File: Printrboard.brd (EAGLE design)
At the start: 100.1 x 61 mm, 119 parts, among them J1 MICROSD, J2 USB-MICROB, J3 ATX, Q1 RFP30N06LE, Q2 RFP30N06LE, Q3 RFP30N06LE, U1 LM2841, U2 A4982, U3 A4982, U4 A4982, U5 A4982, U6 AT90USB1286, U7 AP7313, U8 TXB0104, X1 8MHz

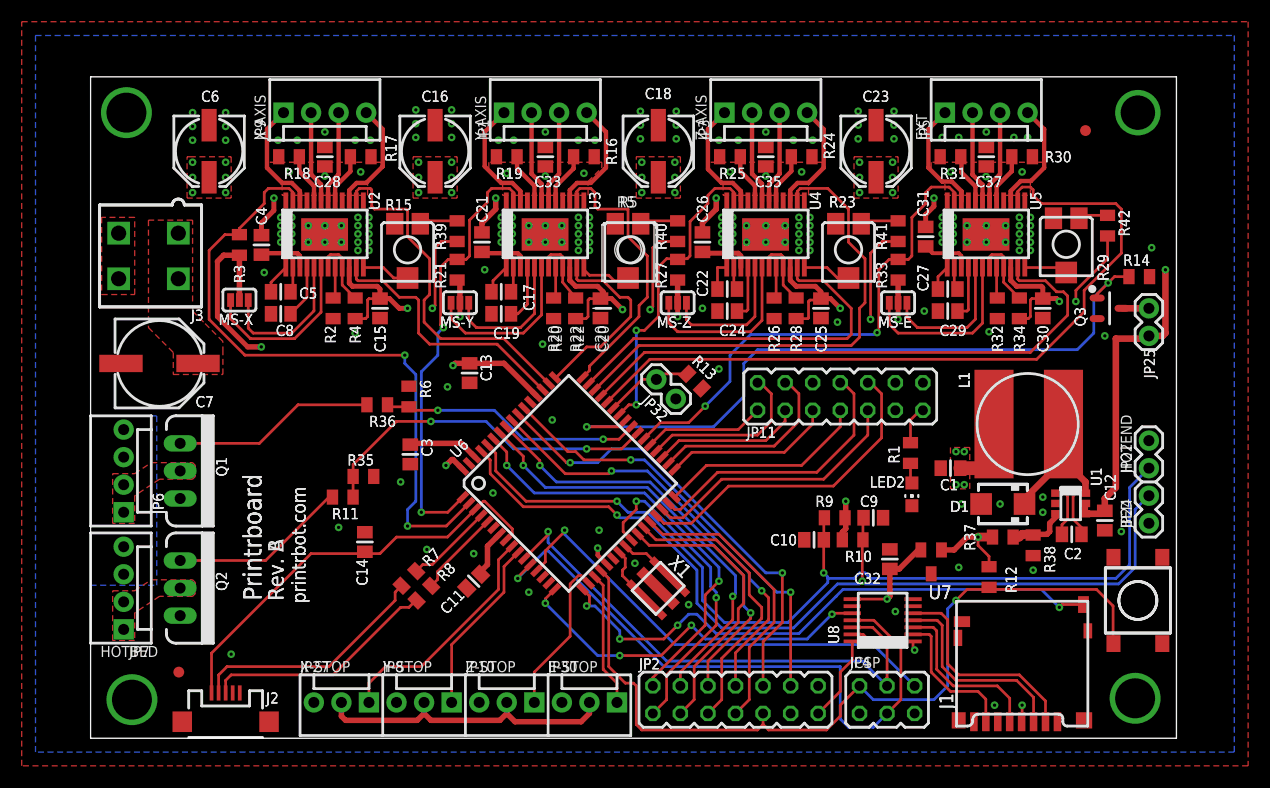
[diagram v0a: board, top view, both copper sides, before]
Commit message: Fix angle errors caused by 6.0 conversion, add more decoupling caps to MCU, and modify some routing
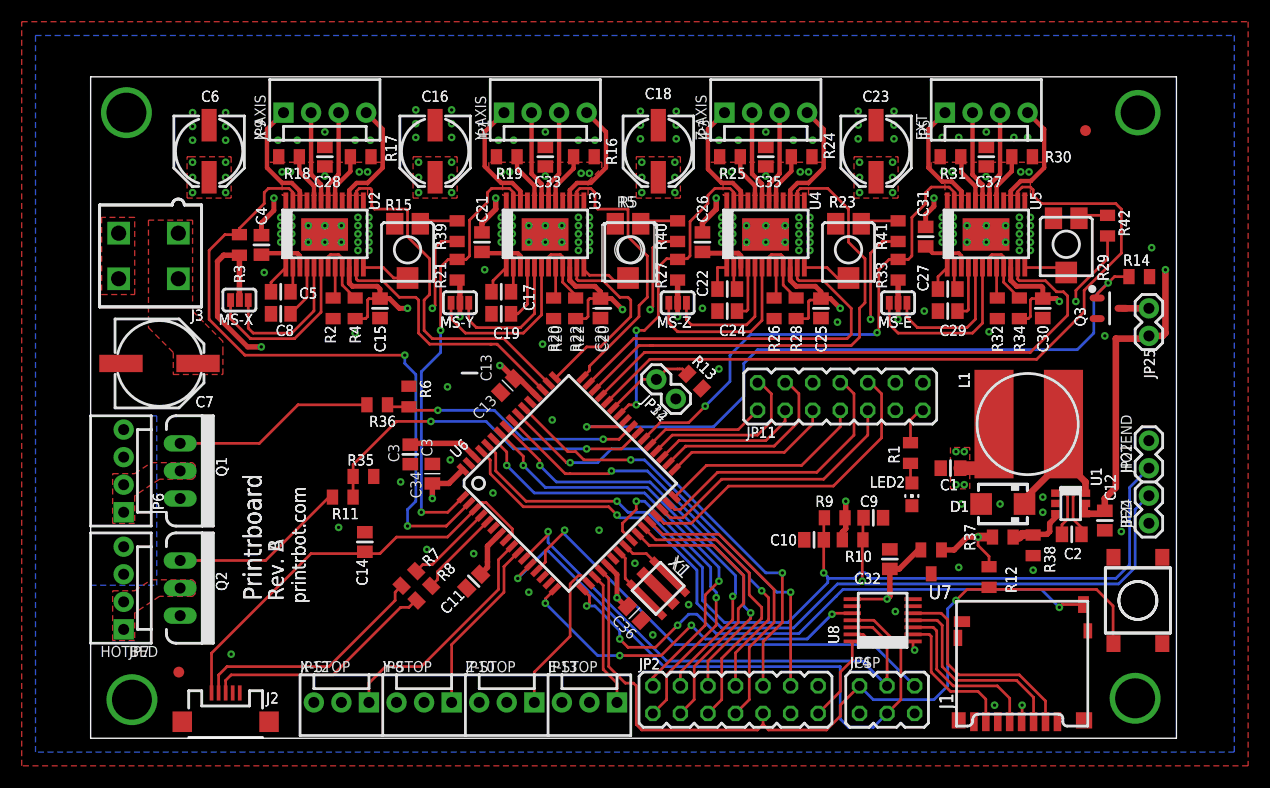
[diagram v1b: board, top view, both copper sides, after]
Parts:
- added C34, C36: 0.1uF, ipc-7351-capacitor:CAPC2012X145AN
- X1: value 8MHz -> 16MHz
- moved C13 3.69 mm to (38.4, 32.5), turned to 45 degrees
- renumbered JP27 to JP12, JP30 to JP13, JP32 to JP14
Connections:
- net +5V: now also C34.2, C36.2
- net GND: now also C34.1, C36.1
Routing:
- net +5V: track 176.9 -> 150.4 mm
- net SDCD: track 53.7 -> 54.5 mm
- net 12V: vias 41 -> 49

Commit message: Change some caps around, add a solder jumper for USB sourced 5V, and modify silkscreen for production
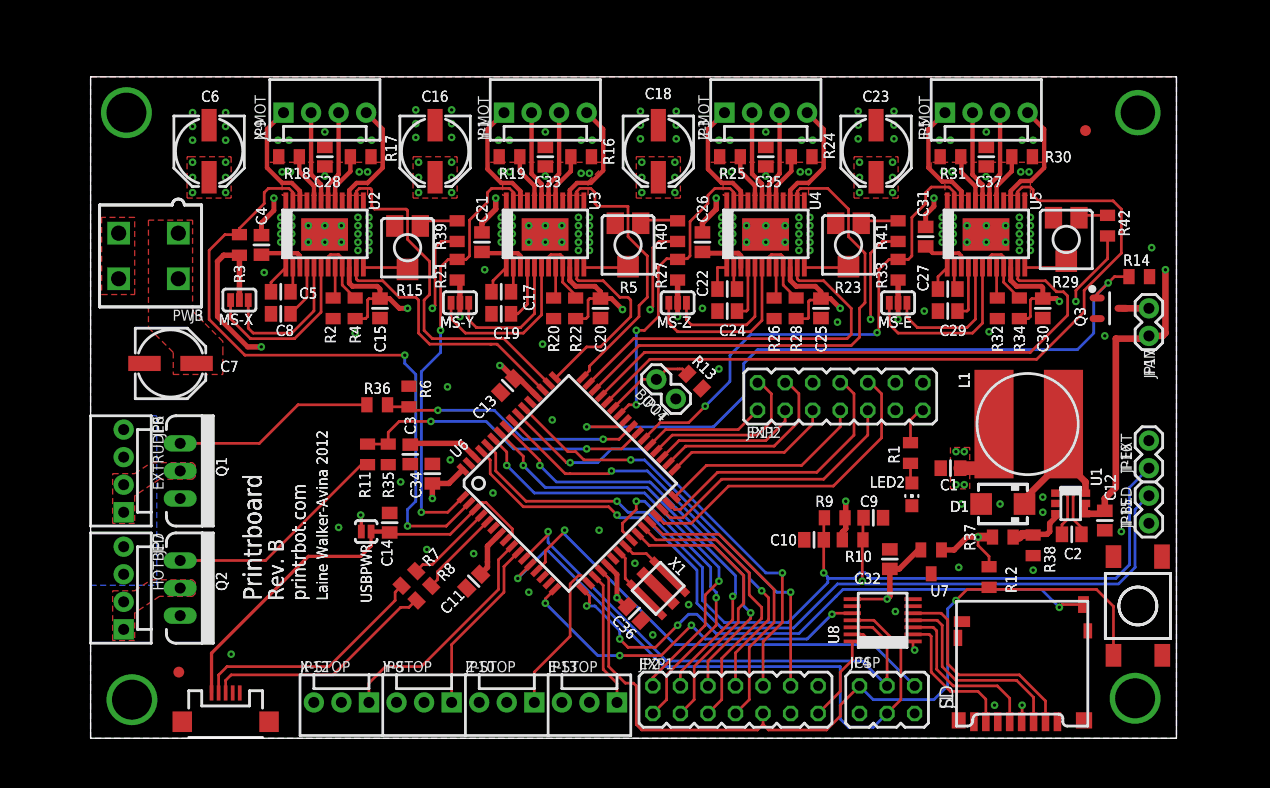
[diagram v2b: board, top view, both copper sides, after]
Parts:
- removed J2: USB-MICROB, SparkFun:USB-MICROB
- removed S2: Reset, SparkFun:TACTILE_SWITCH_TALL
- added S1: Reset, printrbot:TACTILE_SWITCH_TALL
- added USBPWR: (no value), SparkFun:SJ_2S-NO
- added X2: USB-MICROB, printrbot:USB-MICROB
- C32: value 0.1uF -> 10uF
- C7: value 680uF -> 100uF; device rcl:PANASONIC_F -> rcl:PANASONIC_D
- JP11, JP2: value (none) -> EXP
- JP4: value (none) -> ICSP
- R16, R19, R24, R25, R30, R31: value 0.05 -> 0.1
- R17, R18: value 0.05 -> 0.11
- moved R11 4.55 mm to (25.5, 26.2), turned to 270 degrees
- moved R35 3.06 mm to (27.4, 26.2), turned to 270 degrees
- moved R23 3.05 mm to (69.8, 45.5)
- moved R5 3.05 mm to (49.5, 45.5)
- moved R29 3.05 mm to (89.9, 46.0)
- moved C14 2.90 mm to (27.6, 19.9)
- moved R15 2.79 mm to (29.2, 45.2)
- moved C7 1.02 mm to (7.37, 34.5)
- moved R16 0.25 mm to (45.2, 53.6)
- moved R19 0.25 mm to (38.6, 53.6)
- renumbered JP22 to JP16, JP24 to JP15, JP25 to JP17
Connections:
- net !RESET: now also S1.A2; no longer S2.A2
- net +5V: now also USBPWR.2
- net GND: now also S1.B2, X2.GND, X2.MT1, X2.MT2; no longer J2.GND, S2.B2
- net N$2: now also X2.D-; no longer J2.D-
- net N$5: now also X2.D+; no longer J2.D+
- net VBUS: now also USBPWR.1, X2.VBUS; no longer J2.VBUS
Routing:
- net N$7: track 16.5 -> 20.9 mm
- net !HOTBED: track 32.5 -> 28.1 mm
- net +5V: track 150.4 -> 151.9 mm, vias 21 -> 22
- net !RESET: track 77.0 -> 78.1 mm
- net N$33: track 5.05 -> 4.10 mm
- net VBUS: track 39.6 -> 40.5 mm
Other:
- board text added: "/home/ceriand/Downloads/pb-logo.bmp"
- board text added: "BOOT"
- board text added: "C34"
- board text added: "C36"
- board text added: "E-MOT"
- board text added: "EXP1"
- board text added: "EXP2"
- board text added: "EXTRUDER"
- board text added: "FAN"
- board text added: "Laine Walker-Avina 2012"
- board text added: "PWR"
- board text added: "SD"
- board text added: "T-BED"
- board text added: "T-EXT"
- board text added: "USBPWR"
- board text added: "X-MOT"
- board text added: "Y-MOT"
- board text added: "Z-MOT"
- board text removed: "BED"
- board text removed: "EXT"
- board text removed: "HOTEND"
- board text removed: "J1"
- board text removed: "J2"
- board text removed: "J3"
- board text removed: "JP11"
- board text removed: "JP2"
- board text removed: "JP25"
- board text removed: "JP32"
- board text removed: "JP6"
- board text removed: "Rev. A"
- board text removed: "X-AXIS"
- board text removed: "Y-AXIS"
- board text removed: "Z-AXIS"

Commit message: Add extra solder pads for USB connector, and square up mounting holes
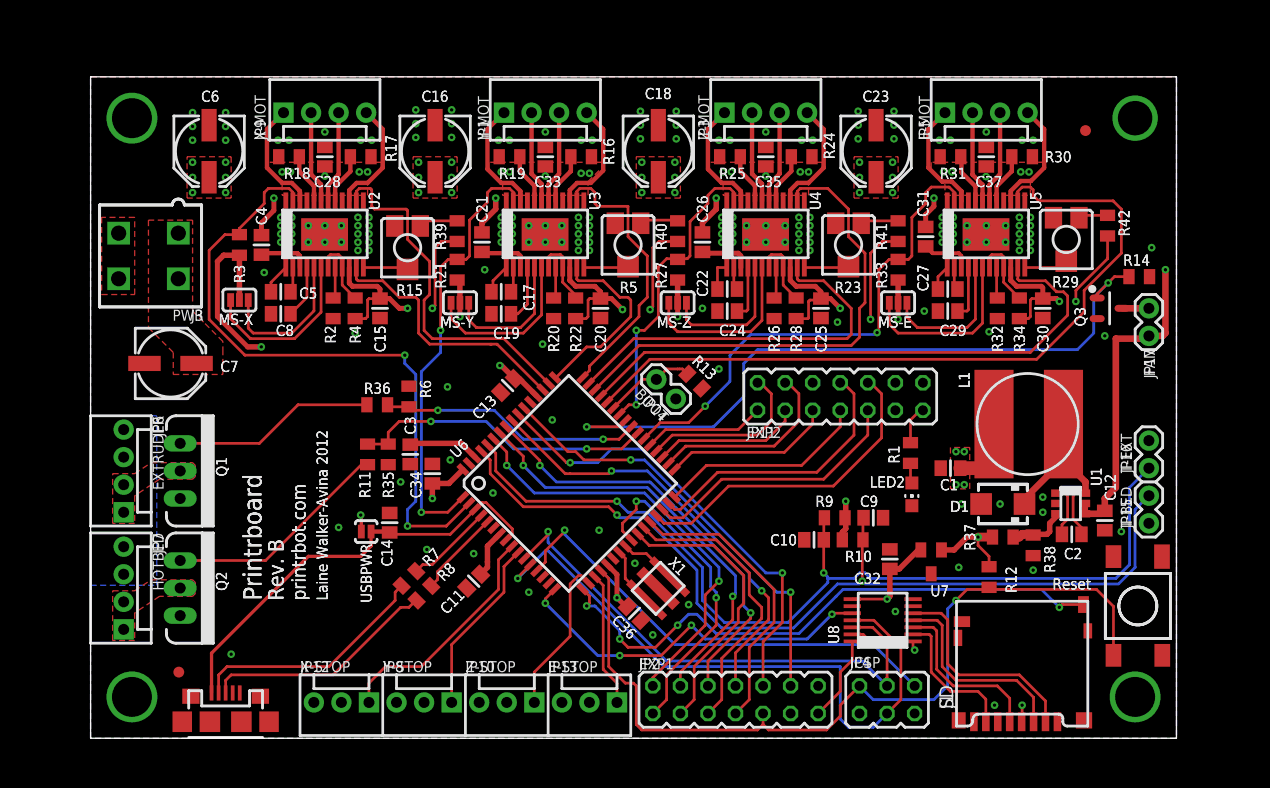
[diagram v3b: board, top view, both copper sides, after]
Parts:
- R37: value 5.49k -> 5.6k
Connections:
- net GND: now also X2.MT3, X2.MT4, X2.MT5, X2.MT6
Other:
- board text added: "Reset"
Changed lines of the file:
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@@
 <?xml version="1.0" encoding="utf-8"?>
 <!DOCTYPE eagle SYSTEM "eagle.dtd">
-<eagle version="6.0">
+<eagle version="6.1">
 <drawing>
 <settings>
@@
 <layer number="23" name="tOrigins" color="15" fill="1" visible="yes" active="yes"/>
 <layer number="24" name="bOrigins" color="15" fill="1" visible="no" active="yes"/>
-<layer number="25" name="tNames" color="7" fill="1" visible="no" active="yes"/>
+<layer number="25" name="tNames" color="7" fill="1" visible="yes" active="yes"/>
 <layer number="26" name="bNames" color="7" fill="1" visible="no" active="yes"/>
 <layer number="27" name="tValues" color="7" fill="1" visible="no" active="yes"/>
 <layer number="28" name="bValues" color="7" fill="1" visible="no" active="yes"/>
-<layer number="29" name="tStop" color="7" fill="1" visible="no" active="yes"/>
+<layer number="29" name="tStop" color="7" fill="1" visible="yes" active="yes"/>
 <layer number="30" name="bStop" color="7" fill="1" visible="no" active="yes"/>
 <layer number="31" name="tCream" color="7" fill="4" visible="no" active="yes"/>
@@
 <layer number="209" name="209bmp" color="7" fill="1" visible="no" active="yes"/>
 <layer number="210" name="210bmp" color="7" fill="1" visible="no" active="yes"/>
+<layer number="211" name="211bmp" color="7" fill="1" visible="no" active="yes"/>
 <layer number="212" name="212bmp" color="7" fill="1" visible="no" active="yes"/>
 <layer number="213" name="213bmp" color="7" fill="1" visible="no" active="yes"/>
@@
 <wire x1="10.246003125" y1="2.974009375" x2="14.645996875" y2="2.974009375" width="0.254" layer="121"/>
 <wire x1="14.645996875" y1="2.974009375" x2="14.645996875" y2="4.37400625" width="0.254" layer="121"/>
+<text x="88.646" y="13.716" size="1.016" layer="25" font="vector" ratio="20">Reset</text>
+<text x="88.646" y="13.716" size="1.016" layer="121" font="vector" ratio="20">Reset</text>
 </plain>
 <attributes>
@@
 <attribute name="VALUE" x="83.971" y="18.666" size="1.27" layer="27"/>
 </element>
-<element name="R37" library="ipc-7351-resistor" package="RESC2012X70N" value="5.49k" x="84.074" y="18.542" smashed="yes">
+<element name="R37" library="ipc-7351-resistor" package="RESC2012X70N" value="5.6k" x="84.074" y="18.542" smashed="yes">
 <attribute name="NAME" x="80.5195" y="19.763" size="1.016" layer="25" font="vector" ratio="20" rot="R270"/>
 <attribute name="VALUE" x="82.599" y="16.2545" size="1.27" layer="27" font="vector" ratio="10"/>
@@
 <via x="22.86" y="19.431" extent="1-16" drill="0.3048"/>
 <via x="28.575" y="23.622" extent="1-16" drill="0.3048"/>
-<via x="96.266" y="3.683" extent="1-16" drill="3.683"/>
-<via x="3.81" y="3.556" extent="1-16" drill="3.683"/>
-<via x="3.302" y="57.658" extent="1-16" drill="3.683"/>
-<via x="96.52" y="57.658" extent="1-16" drill="3.175"/>
+<via x="96.266" y="3.81" extent="1-16" drill="3.683"/>
+<via x="3.81" y="3.81" extent="1-16" drill="3.683"/>
+<via x="3.81" y="57.15" extent="1-16" drill="3.683"/>
+<via x="96.266" y="57.15" extent="1-16" drill="3.175"/>
 <via x="17.272" y="55.118" extent="1-16" drill="0.3048"/>
 <via x="25.908" y="55.118" extent="1-16" drill="0.3048"/>
@@
 <contactref element="C7" pad="-"/>
 <contactref element="S1" pad="B2"/>
+<contactref element="X2" pad="MT3"/>
+<contactref element="X2" pad="MT4"/>
+<contactref element="X2" pad="MT5"/>
+<contactref element="X2" pad="MT6"/>
 </signal>
 <signal name="!RESET">

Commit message: Fixes for Rev C
-Made all mounting holes the same size
-Changed package for stepper solder jumpers to be connected by copper by
default
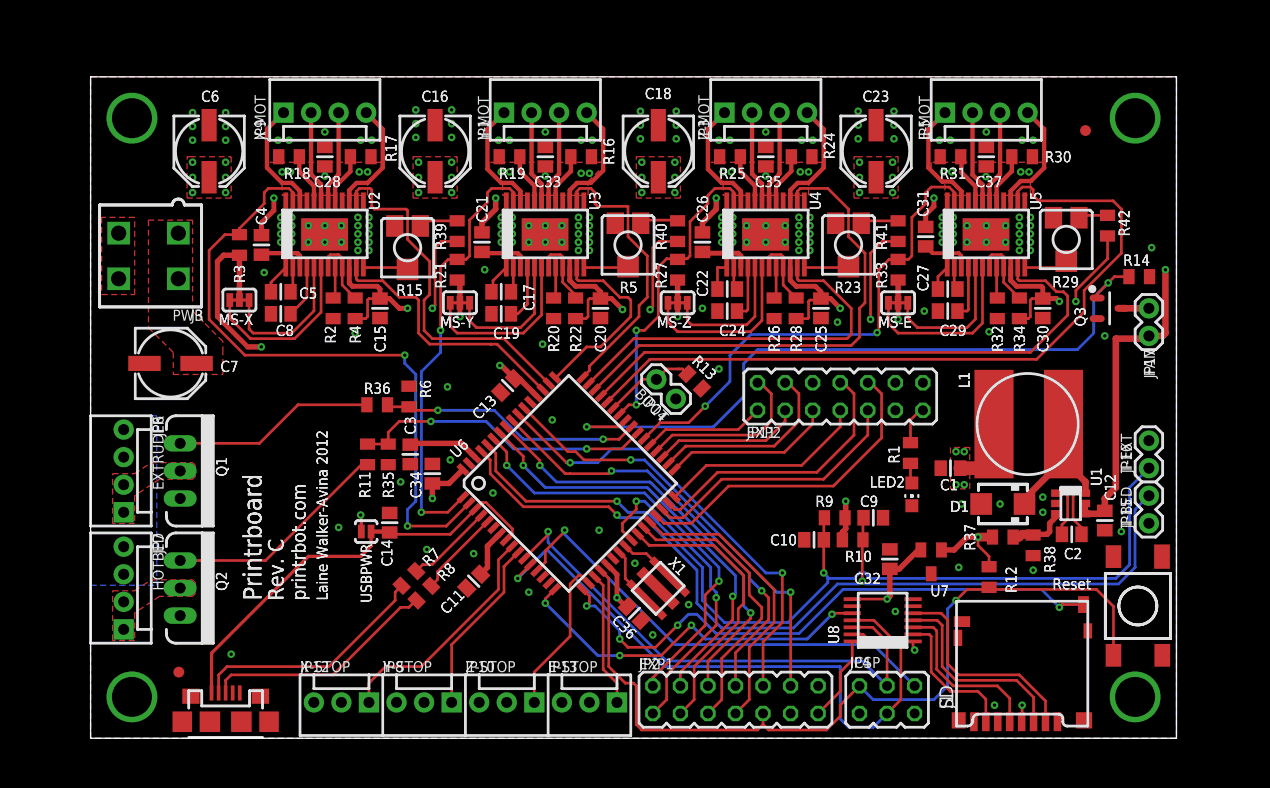
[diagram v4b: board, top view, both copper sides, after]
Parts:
- MS-E, MS-X, MS-Y, MS-Z: device printrbot:SJ_3_PASTE_ALL -> printrbot:SJ_3_CONNECTED
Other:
- board text added: "Rev. C"
- board text removed: "/home/ceriand/Downloads/pb-logo.bmp"
- board text removed: "Rev. B"

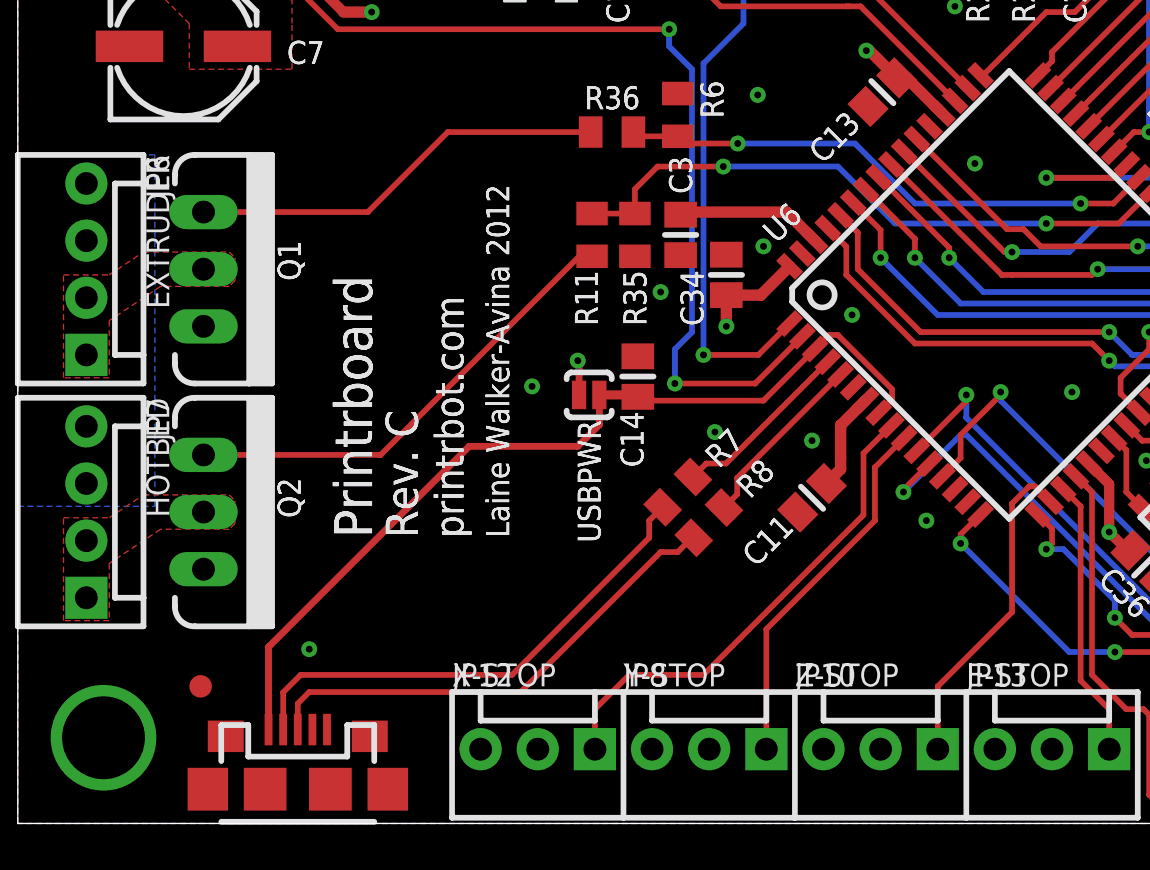
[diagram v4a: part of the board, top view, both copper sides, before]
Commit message: Board tweaks for rev D
Move endstop connectors apart for more clearance and move the labels for
the heaters around so they're easier to see
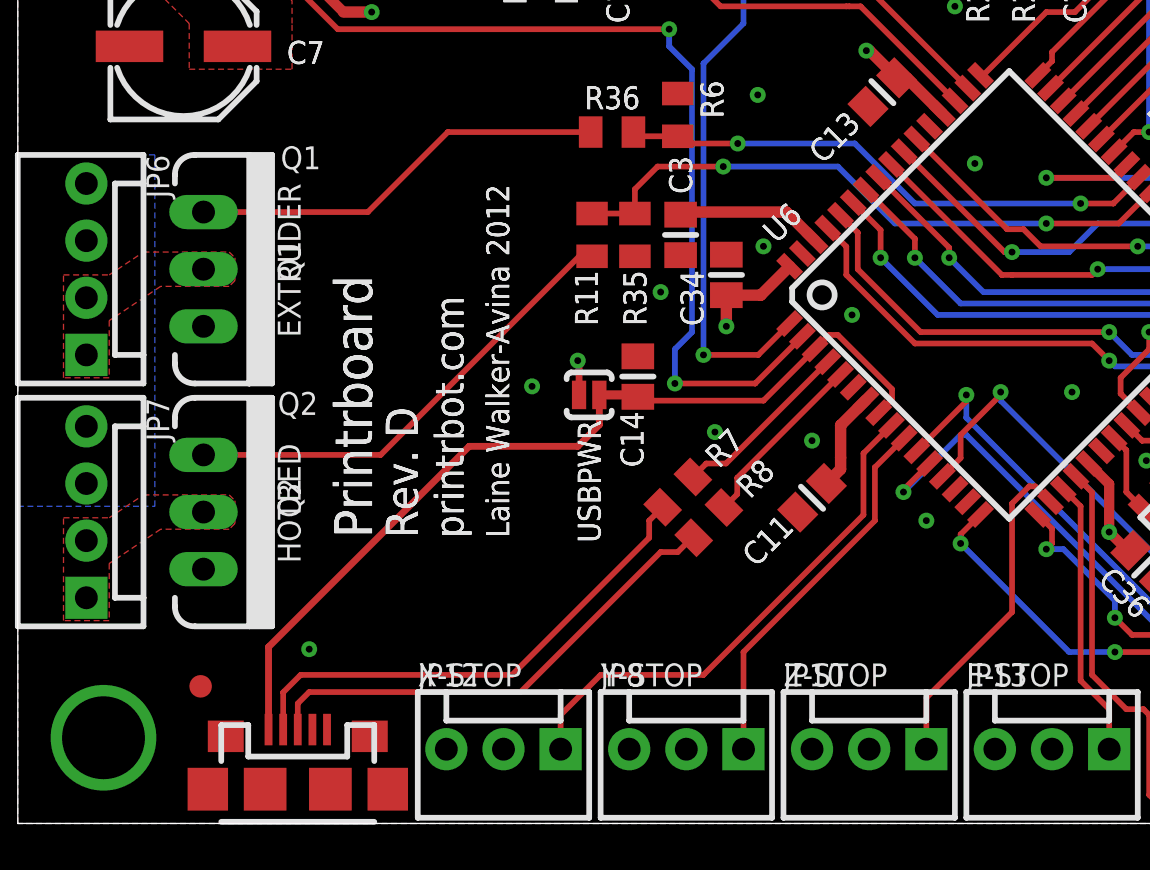
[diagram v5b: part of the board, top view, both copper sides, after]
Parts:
- moved JP12 1.52 mm to (24.1, 3.30)
- moved JP8 1.02 mm to (32.3, 3.30)
- moved JP10 0.51 mm to (40.4, 3.30)
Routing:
- net X-STOP: track 21.8 -> 23.2 mm
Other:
- board text added: "Rev. D"
- board text removed: "Rev. C"
